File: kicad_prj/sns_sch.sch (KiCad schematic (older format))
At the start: 61 parts

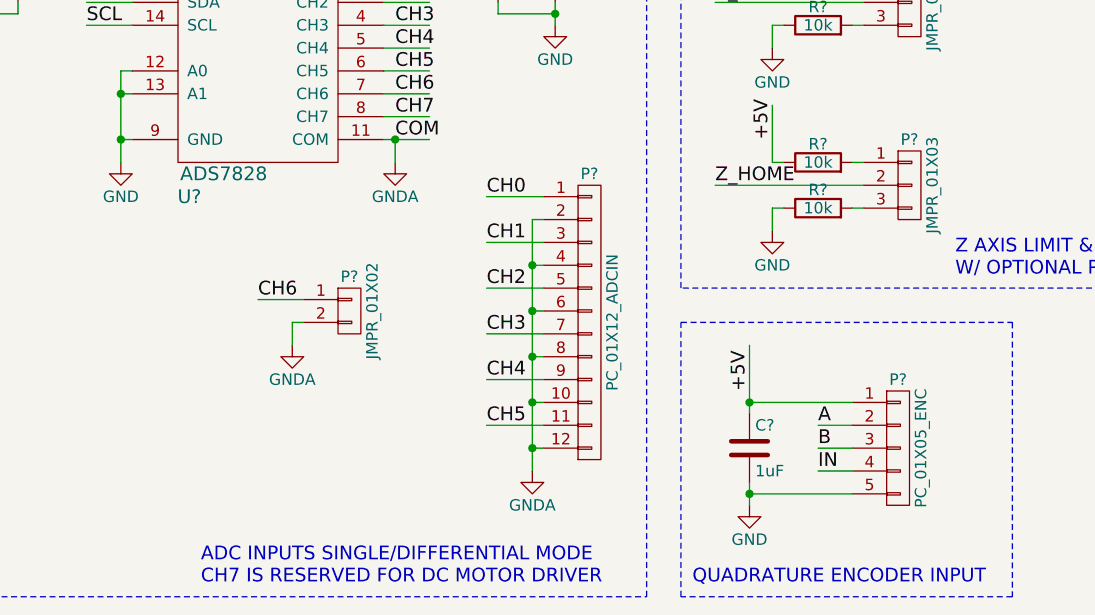
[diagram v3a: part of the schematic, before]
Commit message: Schematics 7
Started power schematics.
Need to:
- correct symbol for sw vreg
- add regulator for 3.3V digital side
- indicate which voltages go to which circuit
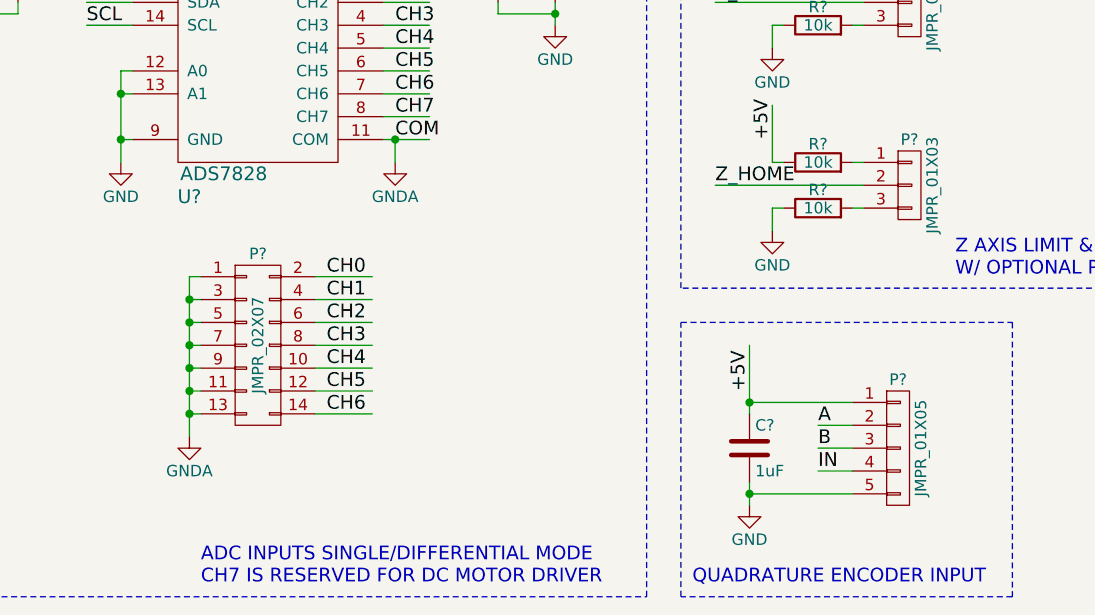
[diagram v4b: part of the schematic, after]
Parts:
- removed P?: JMPR_01X02, symbol JMPR_01X02
- removed P?: PC_01X12_ADCIN, symbol PC_01X12_ADCIN
- removed P?: PC_01X05_ENC, symbol PC_01X05_ENC
- added P?: JMPR_01X05, symbol JMPR_01X05
- added P?: JMPR_02X07, symbol JMPR_02X07
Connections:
- wire segments 236 -> 235
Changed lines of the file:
@@
 $Descr A 11000 8500
 encoding utf-8
-Sheet 7 10
+Sheet 7 11
 Title ""
 Date ""
@@
 F 3 "" H 6900 2150 60  0000 C CNN
 	1    6900 2150
-	1    0    0    -1
-$EndComp
-$Comp
-L PC_01X05_ENC P?
-U 1 1 565A5CD0
-P 5000 6800
-F 0 "P?" H 5000 7100 50  0000 C CNN
-F 1 "PC_01X05_ENC" V 5100 6800 50  0000 C CNN
-F 2 "" H 5000 6800 60  0000 C CNN
-F 3 "" H 5000 6800 60  0000 C CNN
-	1    5000 6800
 	1    0    0    -1
 $EndComp
@@
 GND
 $Comp
-L JMPR_01X02 P?
-U 1 1 56560FF5
-P 2600 6200
-F 0 "P?" H 2600 6350 50  0000 C CNN
-F 1 "JMPR_01X02" V 2700 6200 50  0000 C CNN
-F 2 "" H 2600 6200 60  0000 C CNN
-F 3 "" H 2600 6200 60  0000 C CNN
-	1    2600 6200
-	1    0    0    -1
-$EndComp
-$Comp
-L PC_01X12_ADCIN P?
-U 1 1 565610B4
-P 3650 6250
-F 0 "P?" H 3650 6900 50  0000 C CNN
-F 1 "PC_01X12_ADCIN" V 3750 6250 50  0000 C CNN
-F 2 "" H 3650 6250 60  0000 C CNN
-F 3 "" H 3650 6250 60  0000 C CNN
-	1    3650 6250
-	1    0    0    -1
-$EndComp
-$Comp
 L GNDA #PWR?
 U 1 1 56563772
-P 3400 6900
-F 0 "#PWR?" H 3400 6650 50  0001 C CNN
-F 1 "GNDA" H 3400 6750 50  0000 C CNN
-F 2 "" H 3400 6900 60  0000 C CNN
-F 3 "" H 3400 6900 60  0000 C CNN
-	1    3400 6900
-	1    0    0    -1
-$EndComp
-Text Label 3200 5700 0    60   ~ 0
+P 1900 6750
+F 0 "#PWR?" H 1900 6500 50  0001 C CNN
+F 1 "GNDA" H 1900 6600 50  0000 C CNN
+F 2 "" H 1900 6750 60  0000 C CNN
+F 3 "" H 1900 6750 60  0000 C CNN
+	1    1900 6750
+	1    0    0    -1
+$EndComp
+Text Label 2500 6050 0    60   ~ 0
 CH0
-Text Label 3200 5900 0    60   ~ 0
+Text Label 2500 6150 0    60   ~ 0
 CH1
-Text Label 3200 6100 0    60   ~ 0
+Text Label 2500 6250 0    60   ~ 0
 CH2
-Text Label 3200 6300 0    60   ~ 0
+Text Label 2500 6350 0    60   ~ 0
 CH3
-Text Label 3200 6500 0    60   ~ 0
+Text Label 2500 6450 0    60   ~ 0
 CH4
-Text Label 3200 6700 0    60   ~ 0
+Text Label 2500 6550 0    60   ~ 0
 CH5
-$Comp
-L GNDA #PWR?
-U 1 1 565671B3
-P 2350 6350
-F 0 "#PWR?" H 2350 6100 50  0001 C CNN
-F 1 "GNDA" H 2350 6200 50  0000 C CNN
-F 2 "" H 2350 6350 60  0000 C CNN
-F 3 "" H 2350 6350 60  0000 C CNN
-	1    2350 6350
-	1    0    0    -1
-$EndComp
-Text Label 2200 6150 0    60   ~ 0
+Text Label 2500 6650 0    60   ~ 0
 CH6
 Wire Wire Line
@@
 Connection ~ 2750 3350
 Wire Wire Line
-	3450 5700 3200 5700
-Wire Wire Line
-	3450 5900 3200 5900
-Wire Wire Line
-	3450 6100 3200 6100
-Wire Wire Line
-	3450 6300 3200 6300
-Wire Wire Line
-	3450 6500 3200 6500
-Wire Wire Line
-	3450 6700 3200 6700
-Wire Wire Line
-	3450 5800 3400 5800
-Wire Wire Line
-	3400 5800 3400 6900
-Wire Wire Line
-	3450 6000 3400 6000
-Connection ~ 3400 6000
-Wire Wire Line
-	3450 6200 3400 6200
-Connection ~ 3400 6200
-Wire Wire Line
-	3450 6400 3400 6400
-Connection ~ 3400 6400
-Wire Wire Line
-	3450 6600 3400 6600
-Connection ~ 3400 6600
-Wire Wire Line
-	3450 6800 3400 6800
-Connection ~ 3400 6800
-Wire Wire Line
-	2400 6250 2350 6250
-Wire Wire Line
-	2350 6250 2350 6350
-Wire Wire Line
-	2400 6150 2200 6150
+	2700 6050 2450 6050
+Wire Wire Line
+	2700 6150 2450 6150
+Wire Wire Line
+	2700 6250 2450 6250
+Wire Wire Line
+	2700 6350 2450 6350
+Wire Wire Line
+	2700 6450 2450 6450
+Wire Wire Line
+	2700 6550 2450 6550
+Wire Wire Line
+	2700 6650 2450 6650
 Wire Notes Line
 	700  4050 700  7450
@@
 	1    0    0    -1
 $EndComp
+$Comp
+L JMPR_01X05 P?
+U 1 1 565BD6CC
+P 5000 6800
+F 0 "P?" H 5000 7100 50  0000 C CNN
+F 1 "JMPR_01X05" V 5100 6800 50  0000 C CNN
+F 2 "" H 5000 6800 60  0000 C CNN
+F 3 "" H 5000 6800 60  0000 C CNN
+	1    5000 6800
+	1    0    0    -1
+$EndComp
+$Comp
+L JMPR_02X07 P?
+U 1 1 565BF710
+P 2200 6350
+F 0 "P?" H 2200 6750 50  0000 C CNN
+F 1 "JMPR_02X07" V 2200 6350 50  0000 C CNN
+F 2 "" H 2200 5150 60  0000 C CNN
+F 3 "" H 2200 5150 60  0000 C CNN
+	1    2200 6350
+	1    0    0    -1
+$EndComp
+Wire Wire Line
+	1950 6050 1900 6050
+Wire Wire Line
+	1900 6050 1900 6750
+Wire Wire Line
+	1950 6150 1900 6150
+Connection ~ 1900 6150
+Wire Wire Line
+	1950 6250 1900 6250
+Connection ~ 1900 6250
+Wire Wire Line
+	1950 6350 1900 6350
+Connection ~ 1900 6350
+Wire Wire Line
+	1950 6450 1900 6450
+Connection ~ 1900 6450
+Wire Wire Line
+	1950 6550 1900 6550
+Connection ~ 1900 6550
+Wire Wire Line
+	1950 6650 1900 6650
+Connection ~ 1900 6650
 $EndSCHEMATC

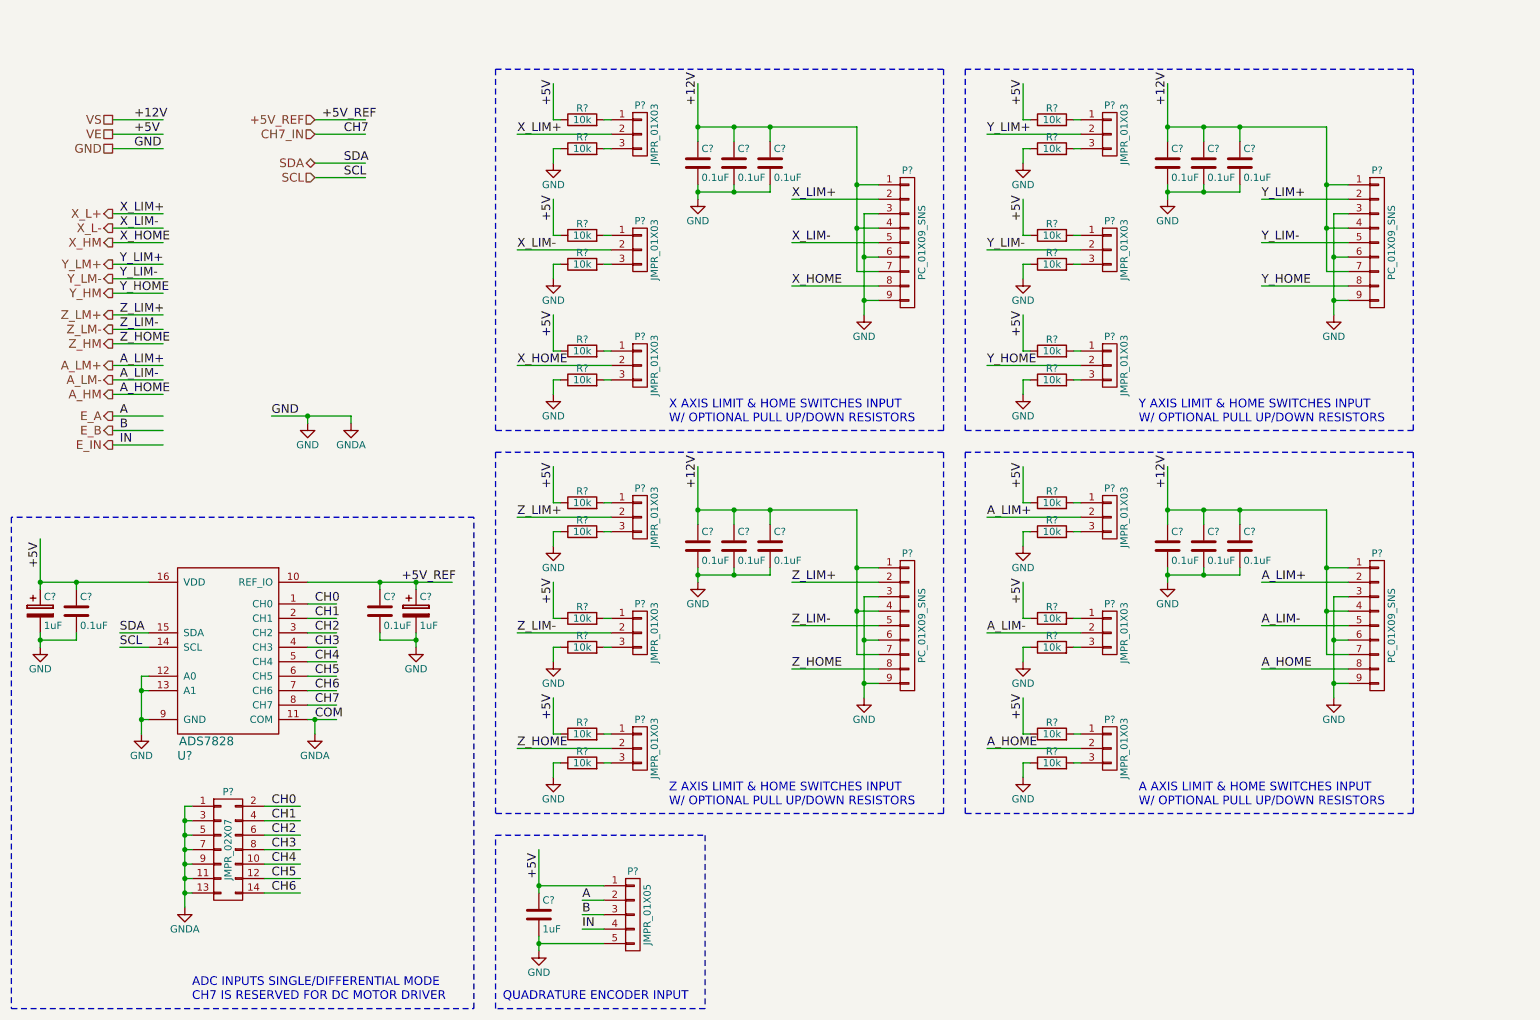
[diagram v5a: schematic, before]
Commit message: Buffers for limit switches
Added buffers and filters.
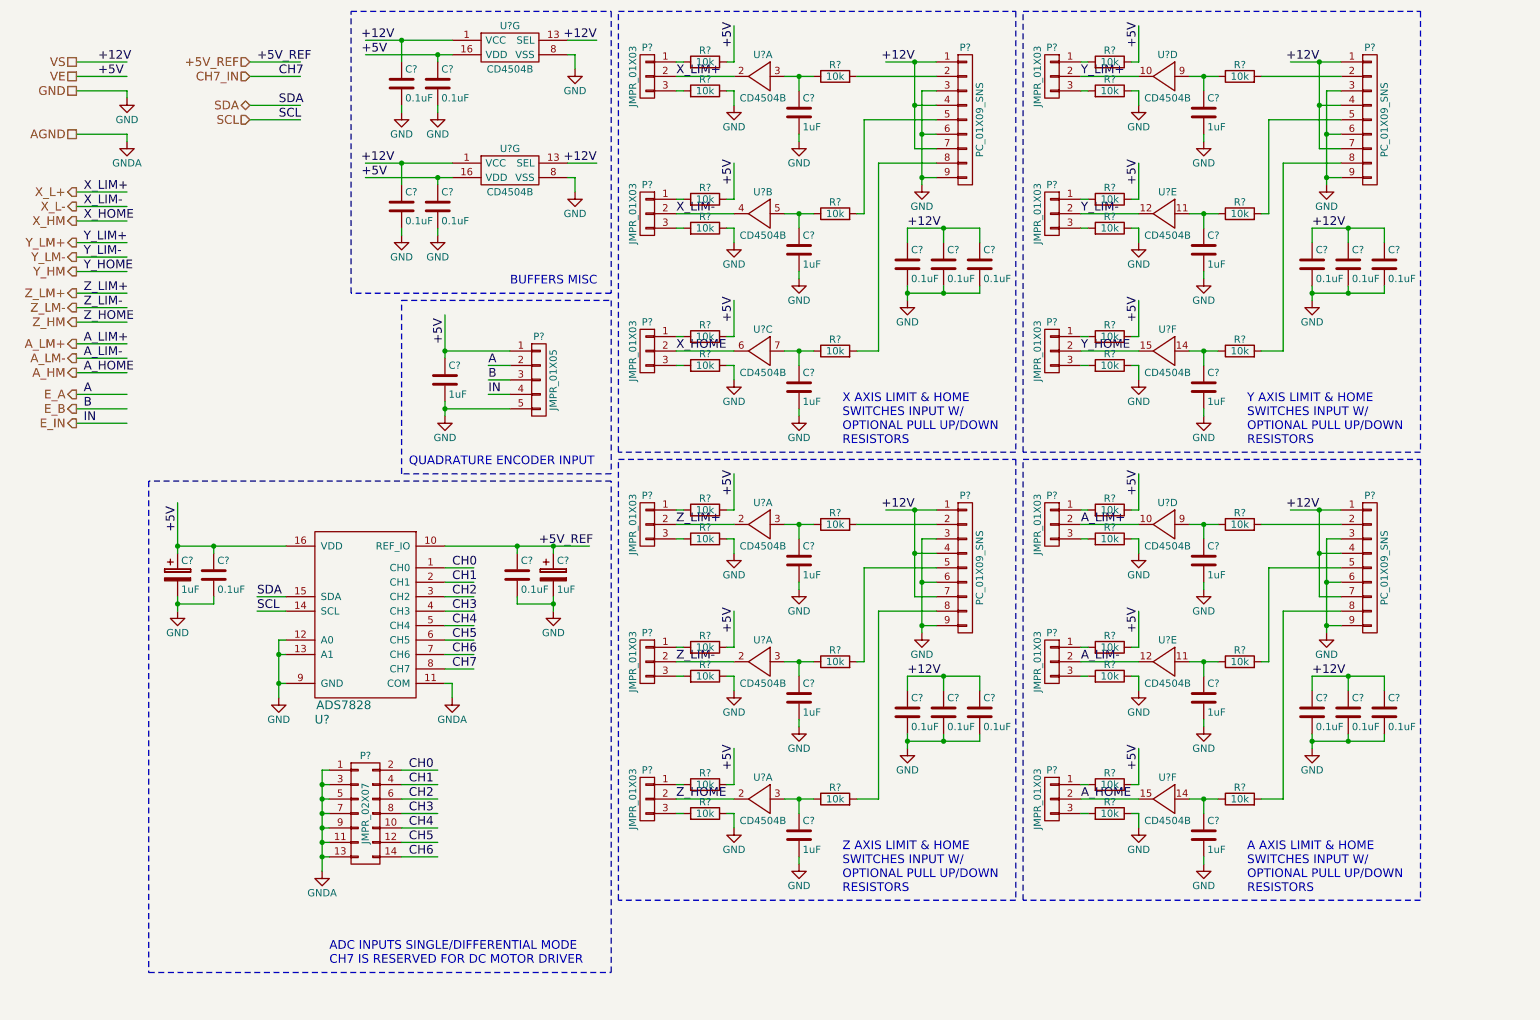
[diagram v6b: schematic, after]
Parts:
- removed C? (x9): 0.1uF, symbol C
- removed P? (x3): PC_01X09_SNS, symbol PC_01X09_SNS
- removed P? (x9): JMPR_01X03, symbol JMPR_01X03
- removed R? (x18): 10k, symbol R
- added C? (x12): 1uF, symbol C
- added C? (x13): 0.1uF, symbol C
- added P? (x3): PC_01X09_SNS, symbol PC_01X09_SNS
- added P? (x9): JMPR_01X03, symbol JMPR_01X03
- added R? (x30): 10k, symbol R
- added U? (x14): CD4504B, symbol CD4504B
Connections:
- net labels added: AGND
- net labels removed: COM
- wire segments 235 -> 305
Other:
- note added: "A AXIS LIMIT & HOME \nSWITCHES INPUT W/ \nOPTIONAL PULL UP/DOWN \nRESISTORS\n\n"
- note added: "BUFFERS MISC\n"
- note added: "X AXIS LIMIT & HOME \nSWITCHES INPUT W/ \nOPTIONAL PULL UP/DOWN \nRESISTORS\n\n"
- note added: "Y AXIS LIMIT & HOME \nSWITCHES INPUT W/ \nOPTIONAL PULL UP/DOWN \nRESISTORS\n\n"
- note added: "Z AXIS LIMIT & HOME \nSWITCHES INPUT W/ \nOPTIONAL PULL UP/DOWN \nRESISTORS\n\n"
- note removed: "A AXIS LIMIT & HOME SWITCHES INPUT\nW/ OPTIONAL PULL UP/DOWN RESISTORS\n\n"
- note removed: "X AXIS LIMIT & HOME SWITCHES INPUT\nW/ OPTIONAL PULL UP/DOWN RESISTORS\n\n"
- note removed: "Y AXIS LIMIT & HOME SWITCHES INPUT\nW/ OPTIONAL PULL UP/DOWN RESISTORS\n\n"
- note removed: "Z AXIS LIMIT & HOME SWITCHES INPUT\nW/ OPTIONAL PULL UP/DOWN RESISTORS\n\n"
- moved on the sheet: C?, P?, R?, U?
